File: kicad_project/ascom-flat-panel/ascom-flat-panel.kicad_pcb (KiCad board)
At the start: 4 copper layers, 55 x 29.5 mm, 13 parts, among them Q1 FQP30N06L, Q2 FQP30N06L

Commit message: optimisation (rotation de diode)
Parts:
- moved D2 10.2 mm to (109.0, 82.1), turned to 90 degrees
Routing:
- net SERVO GND: track 25.6 -> 27.7 mm
- net SERVO VCC: track 18.4 -> 16.9 mm
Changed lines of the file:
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@@
 			)
 		)
+		(model "C:/Users/dell/Documents/GitHub/ascom-flat-panel/kicad_project/seeeduino-xiao-samd21-3d-model/Seeeduino XIAO SAMD21 v4.step"
+			(offset
+				(xyz 0 0 0)
+			)
+			(scale
+				(xyz 1 1 1)
+			)
+			(rotate
+				(xyz -0 -0 -90)
+			)
+		)
 	)
 	(footprint "Diode_THT:D_DO-41_SOD81_P10.16mm_Horizontal"
@@
 	(footprint "Diode_THT:D_DO-41_SOD81_P10.16mm_Horizontal"
 		(layer "F.Cu")
-		(at 109 71.92 -90)
+		(at 109 82.08 90)
 		(descr "Diode, DO-41_SOD81 series, Axial, Horizontal, pin pitch=10.16mm, , length*diameter=5.2*2.7mm^2, , http://www.diodes.com/_files/packages/DO-41%20(Plastic).pdf")
 		(tags "Diode DO-41_SOD81 series Axial Horizontal pin pitch 10.16mm  length 5.2mm diameter 2.7mm")
 		(property "Reference" "D2"
-			(at 5.08 2.5 90)
+			(at 5.08 -2.5 90)
 			(layer "F.SilkS")
 			(effects
@@
 		)
 		(property "Datasheet" "http://www.vishay.com/docs/88503/1n4001.pdf"
-			(at 0 0 270)
+			(at 0 0 90)
 			(unlocked yes)
 			(layer "F.Fab")
@@
 		)
 		(property "Description" ""
-			(at 0 0 270)
+			(at 0 0 90)
 			(unlocked yes)
 			(layer "F.Fab")
@@
 		)
 		(property "Sim.Device" "D"
-			(at 0 0 270)
+			(at 0 0 90)
 			(unlocked yes)
 			(layer "F.Fab")
@@
 		)
 		(property "Sim.Pins" "1=K 2=A"
-			(at 0 0 270)
+			(at 0 0 90)
 			(unlocked yes)
 			(layer "F.Fab")
@@
 		(attr through_hole)
 		(fp_line
-			(start 2.36 1.47)
-			(end 7.8 1.47)
+			(start 7.8 -1.47)
+			(end 2.36 -1.47)
 			(stroke
 				(width 0.12)
@@
 		)
 		(fp_line
-			(start 7.8 1.47)
-			(end 7.8 -1.47)
+			(start 3.38 -1.47)
+			(end 3.38 1.47)
 			(stroke
 				(width 0.12)
@@
 		)
 		(fp_line
-			(start 1.34 0)
-			(end 2.36 0)
+			(start 3.26 -1.47)
+			(end 3.26 1.47)
 			(stroke
 				(width 0.12)
@@
 		)
 		(fp_line
-			(start 8.82 0)
-			(end 7.8 0)
+			(start 3.14 -1.47)
+			(end 3.14 1.47)
 			(stroke
 				(width 0.12)
@@
 		)
 		(fp_line
-			(start 3.14 -1.47)
-			(end 3.14 1.47)
+			(start 8.82 0)
+			(end 7.8 0)
 			(stroke
 				(width 0.12)
@@
 		)
 		(fp_line
-			(start 3.26 -1.47)
-			(end 3.26 1.47)
+			(start 1.34 0)
+			(end 2.36 0)
 			(stroke
 				(width 0.12)
@@
 		)
 		(fp_line
-			(start 3.38 -1.47)
-			(end 3.38 1.47)
+			(start 7.8 1.47)
+			(end 7.8 -1.47)
 			(stroke
 				(width 0.12)
@@
 		)
 		(fp_line
-			(start 7.8 -1.47)
-			(end 2.36 -1.47)
+			(start 2.36 1.47)
+			(end 7.8 1.47)
 			(stroke
 				(width 0.12)
@@
 		)
 		(fp_line
-			(start -1.35 1.6)
-			(end 11.51 1.6)
+			(start 11.51 -1.6)
+			(end -1.35 -1.6)
 			(stroke
 				(width 0.05)
@@
 		)
 		(fp_line
-			(start 11.51 1.6)
-			(end 11.51 -1.6)
+			(start -1.35 -1.6)
+			(end -1.35 1.6)
 			(stroke
 				(width 0.05)
@@
 		)
 		(fp_line
-			(start -1.35 -1.6)
-			(end -1.35 1.6)
+			(start 11.51 1.6)
+			(end 11.51 -1.6)
 			(stroke
 				(width 0.05)
@@
 		)
 		(fp_line
-			(start 11.51 -1.6)
-			(end -1.35 -1.6)
+			(start -1.35 1.6)
+			(end 11.51 1.6)
 			(stroke
 				(width 0.05)
@@
 		)
 		(fp_line
-			(start 2.48 1.35)
-			(end 7.68 1.35)
+			(start 7.68 -1.35)
+			(end 2.48 -1.35)
 			(stroke
 				(width 0.1)
@@
 		)
 		(fp_line
-			(start 7.68 1.35)
-			(end 7.68 -1.35)
+			(start 3.36 -1.35)
+			(end 3.36 1.35)
 			(stroke
 				(width 0.1)
@@
 		)
 		(fp_line
-			(start 0 0)
-			(end 2.48 0)
+			(start 3.26 -1.35)
+			(end 3.26 1.35)
 			(stroke
 				(width 0.1)
@@
 		)
 		(fp_line
-			(start 10.16 0)
-			(end 7.68 0)
+			(start 3.16 -1.35)
+			(end 3.16 1.35)
 			(stroke
 				(width 0.1)
@@
 		)
 		(fp_line
-			(start 3.16 -1.35)
-			(end 3.16 1.35)
+			(start 10.16 0)
+			(end 7.68 0)
 			(stroke
 				(width 0.1)
@@
 		)
 		(fp_line
-			(start 3.26 -1.35)
-			(end 3.26 1.35)
+			(start 0 0)
+			(end 2.48 0)
 			(stroke
 				(width 0.1)
@@
 		)
 		(fp_line
-			(start 3.36 -1.35)
-			(end 3.36 1.35)
+			(start 7.68 1.35)
+			(end 7.68 -1.35)
 			(stroke
 				(width 0.1)
@@
 		)
 		(fp_line
-			(start 7.68 -1.35)
-			(end 2.48 -1.35)
+			(start 2.48 1.35)
+			(end 7.68 1.35)
 			(stroke
 				(width 0.1)
@@
 		)
 		(pad "1" thru_hole rect
-			(at 0 0 270)
+			(at 0 0 90)
 			(size 2.2 2.2)
 			(drill 1.1)
@@
 		)
 		(pad "2" thru_hole oval
-			(at 10.16 0 270)
+			(at 10.16 0 90)
 			(size 2.2 2.2)
 			(drill 1.1)
@@
 	)
 	(segment
-		(start 109 76.58)
-		(end 114.5 82.08)
+		(start 114.5 82.08)
+		(end 109 82.08)
 		(width 0.4)
 		(layer "B.Cu")
@@
 	)
 	(segment
-		(start 109 71.92)
-		(end 104.5 71.92)
+		(start 103.5 73)
+		(end 103.5 72.92)
 		(width 0.4)
 		(layer "B.Cu")
@@
 	)
 	(segment
-		(start 109 71.92)
-		(end 109 76.58)
+		(start 109 78.5)
+		(end 103.5 73)
 		(width 0.4)
 		(layer "B.Cu")
@@
 	)
 	(segment
-		(start 104.5 71.92)
-		(end 103.5 72.92)
+		(start 109 82.08)
+		(end 109 78.5)
 		(width 0.4)
 		(layer "B.Cu")
@@
 	)
 	(segment
+		(start 102.299 74.259)
+		(end 103.5 75.46)
+		(width 0.4)
+		(layer "B.Cu")
+		(net 4)
+	)
+	(segment
+		(start 102.299 71.719)
+		(end 102.299 74.259)
+		(width 0.4)
+		(layer "B.Cu")
+		(net 4)
+	)
+	(segment
 		(start 102.299 76.661)
 		(end 103.5 75.46)
@@
 	)
 	(segment
-		(start 103.945 91)
-		(end 102.299 89.354)
+		(start 108.799 71.719)
+		(end 102.299 71.719)
 		(width 0.4)
 		(layer "B.Cu")
@@
 	)
 	(segment
-		(start 109 82.08)
-		(end 109 80.96)
+		(start 109 71.92)
+		(end 108.799 71.719)
 		(width 0.4)
 		(layer "B.Cu")
@@
 	)
 	(segment
-		(start 109 80.96)
-		(end 103.5 75.46)
+		(start 103.945 91)
+		(end 102.299 89.354)
 		(width 0.4)
 		(layer "B.Cu")

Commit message: correction suite à détection d'erreur...
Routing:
- net SERVO POSITION CONTROL: track 21.3 -> 22.4 mm
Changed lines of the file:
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@@
 	)
 	(segment
-		(start 111.980397 86.971)
-		(end 103.5 78.490603)
+		(start 111.537339 86.971)
+		(end 108.566339 84)
+		(width 0.2)
+		(layer "B.Cu")
+		(net 6)
+	)
+	(segment
+		(start 108.566339 84)
+		(end 108 84)
 		(width 0.2)
 		(layer "B.Cu")
@@
 	(segment
 		(start 119.009 86.971)
-		(end 111.980397 86.971)
+		(end 111.537339 86.971)
 		(width 0.2)
 		(layer "B.Cu")
@@
 		(width 0.2)
 		(layer "B.Cu")
+		(net 6)
+	)
+	(segment
+		(start 105.5 81.5)
+		(end 105.5 80)
+		(width 0.2)
+		(layer "B.Cu")
+		(net 6)
+	)
+	(segment
+		(start 105.5 80)
+		(end 103.5 78)
+		(width 0.2)
+		(layer "B.Cu")
+		(net 6)
+	)
+	(segment
+		(start 108 84)
+		(end 105.5 81.5)
+		(width 0.2)
+		(layer "B.Cu")

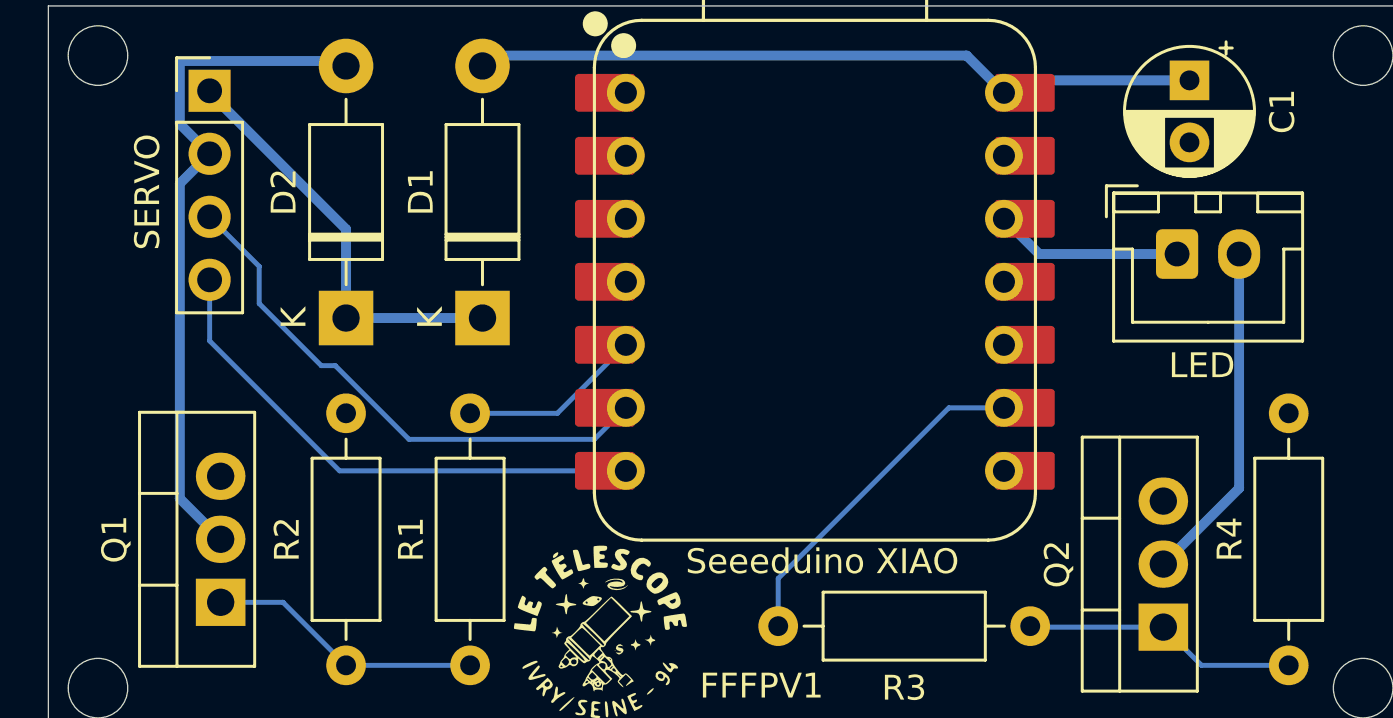
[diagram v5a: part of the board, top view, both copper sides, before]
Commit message: Corrections de routage pour améliorer les connexions à la masse
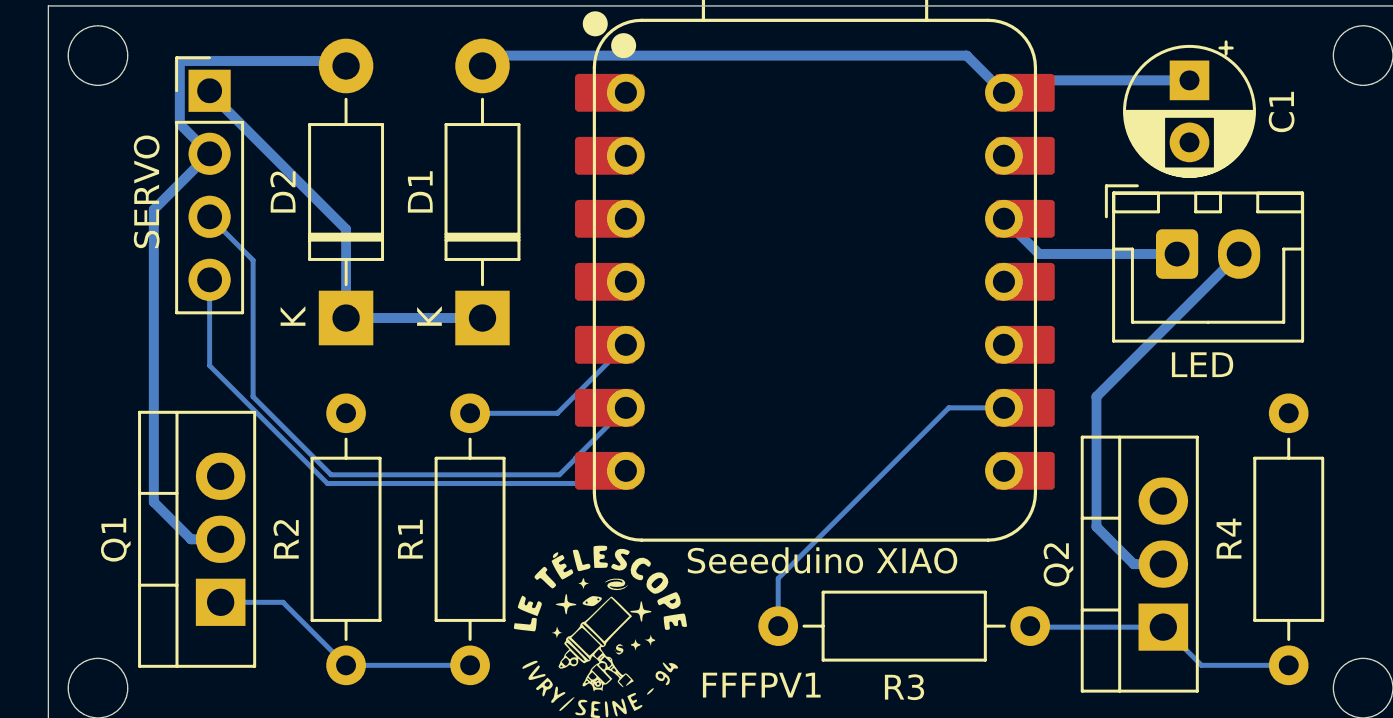
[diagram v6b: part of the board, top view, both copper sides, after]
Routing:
- net SERVO POSITION CONTROL: track 22.4 -> 25.9 mm
- net Net-(J3-Pin_2): track 13.8 -> 16.7 mm
- net SERVO GND: track 27.7 -> 29.3 mm
- net SERVO POSITION FEEDBACK: track 21.4 -> 22.4 mm
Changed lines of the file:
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@@
 	)
 	(segment
-		(start 102.299 76.661)
-		(end 103.5 75.46)
+		(start 108.799 71.719)
+		(end 102.299 71.719)
 		(width 0.4)
 		(layer "B.Cu")
@@
 	)
 	(segment
-		(start 108.799 71.719)
-		(end 102.299 71.719)
+		(start 101.25 89.5)
+		(end 101.25 77.71)
 		(width 0.4)
 		(layer "B.Cu")
@@
 	)
 	(segment
-		(start 103.945 91)
-		(end 102.299 89.354)
+		(start 101.25 77.71)
+		(end 103.5 75.46)
 		(width 0.4)
 		(layer "B.Cu")
@@
 	)
 	(segment
-		(start 102.299 89.354)
-		(end 102.299 76.661)
+		(start 103.945 91)
+		(end 102.75 91)
 		(width 0.4)
 		(layer "B.Cu")
@@
 	)
 	(segment
-		(start 120.28 88.24)
-		(end 108.74 88.24)
+		(start 102.75 91)
+		(end 101.25 89.5)
+		(width 0.4)
+		(layer "B.Cu")
+		(net 4)
+	)
+	(segment
+		(start 119.77 88.75)
+		(end 108.25 88.75)
 		(width 0.2)
 		(layer "B.Cu")
@@
 	)
 	(segment
-		(start 103.5 83)
-		(end 103.5 80.54)
+		(start 108.25 88.75)
+		(end 103.5 84)
 		(width 0.2)
 		(layer "B.Cu")
@@
 	)
 	(segment
-		(start 108.74 88.24)
-		(end 103.5 83)
+		(start 120.28 88.24)
+		(end 119.77 88.75)
+		(width 0.2)
+		(layer "B.Cu")
+		(net 5)
+	)
+	(segment
+		(start 103.5 84)
+		(end 103.5 80.54)
 		(width 0.2)
 		(layer "B.Cu")
@@
 	)
 	(segment
-		(start 111.537339 86.971)
-		(end 108.566339 84)
+		(start 117.601 88.399)
+		(end 118.25 87.75)
 		(width 0.2)
 		(layer "B.Cu")
@@
 	)
 	(segment
-		(start 108.566339 84)
-		(end 108 84)
+		(start 118.25 87.73)
+		(end 120.28 85.7)
 		(width 0.2)
 		(layer "B.Cu")
@@
 	)
 	(segment
-		(start 119.009 86.971)
-		(end 111.537339 86.971)
+		(start 103.5 78)
+		(end 105.25 79.75)
 		(width 0.2)
 		(layer "B.Cu")
@@
 	)
 	(segment
-		(start 120.28 85.7)
-		(end 119.009 86.971)
+		(start 108.399 88.399)
+		(end 117.601 88.399)
 		(width 0.2)
 		(layer "B.Cu")
@@
 	)
 	(segment
-		(start 105.5 81.5)
-		(end 105.5 80)
+		(start 105.25 85.25)
+		(end 108.399 88.399)
 		(width 0.2)
 		(layer "B.Cu")
@@
 	)
 	(segment
-		(start 105.5 80)
-		(end 103.5 78)
+		(start 105.25 79.75)
+		(end 105.25 85.25)
 		(width 0.2)
 		(layer "B.Cu")
@@
 	)
 	(segment
-		(start 108 84)
-		(end 105.5 81.5)
-		(width 0.2)
+		(start 118.25 87.75)
+		(end 118.25 87.73)
+		(width 0.15)
 		(layer "B.Cu")
 		(net 6)
@@
 	)
 	(segment
-		(start 141.945 92)
-		(end 145 88.945)
+		(start 139.25 85.25)
+		(end 145 79.5)
 		(width 0.4)
 		(layer "B.Cu")
@@
 	)
 	(segment
-		(start 145 88.945)
-		(end 145 79.5)
+		(start 140.75 92)
+		(end 139.25 90.5)
 		(width 0.4)
 		(layer "B.Cu")
+		(net 8)
+	)
+	(segment
+		(start 141.945 92)
+		(end 140.75 92)
+		(width 0.4)
+		(layer "B.Cu")
+		(net 8)
+	)
+	(segment
+		(start 139.25 90.5)
+		(end 139.25 85.25)
+		(width 0.4)
+		(layer "B.Cu")

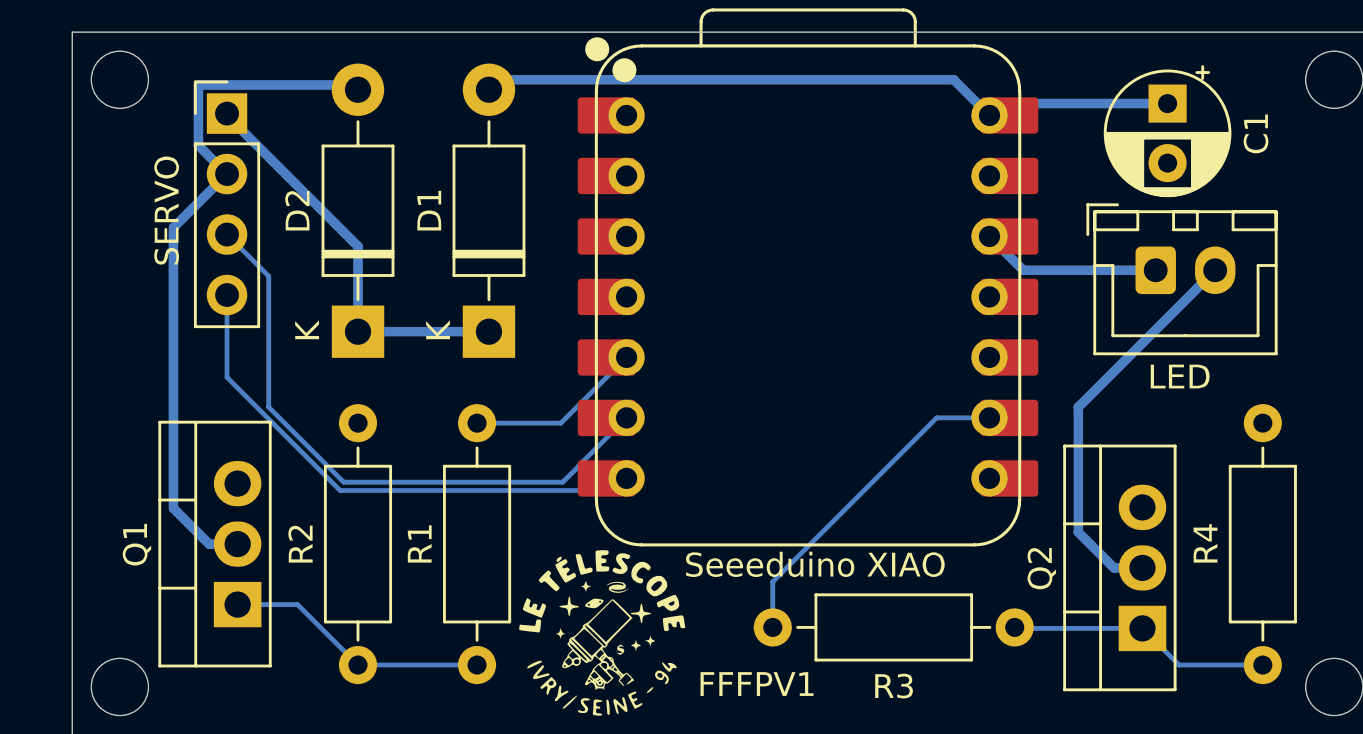
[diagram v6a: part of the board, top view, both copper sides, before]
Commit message: Mise à jour des références des diodes et MOSFET suivant composants achetés. TODO : vérifier pas et diamètre de C1 - ajuster empreinte le cas échéant
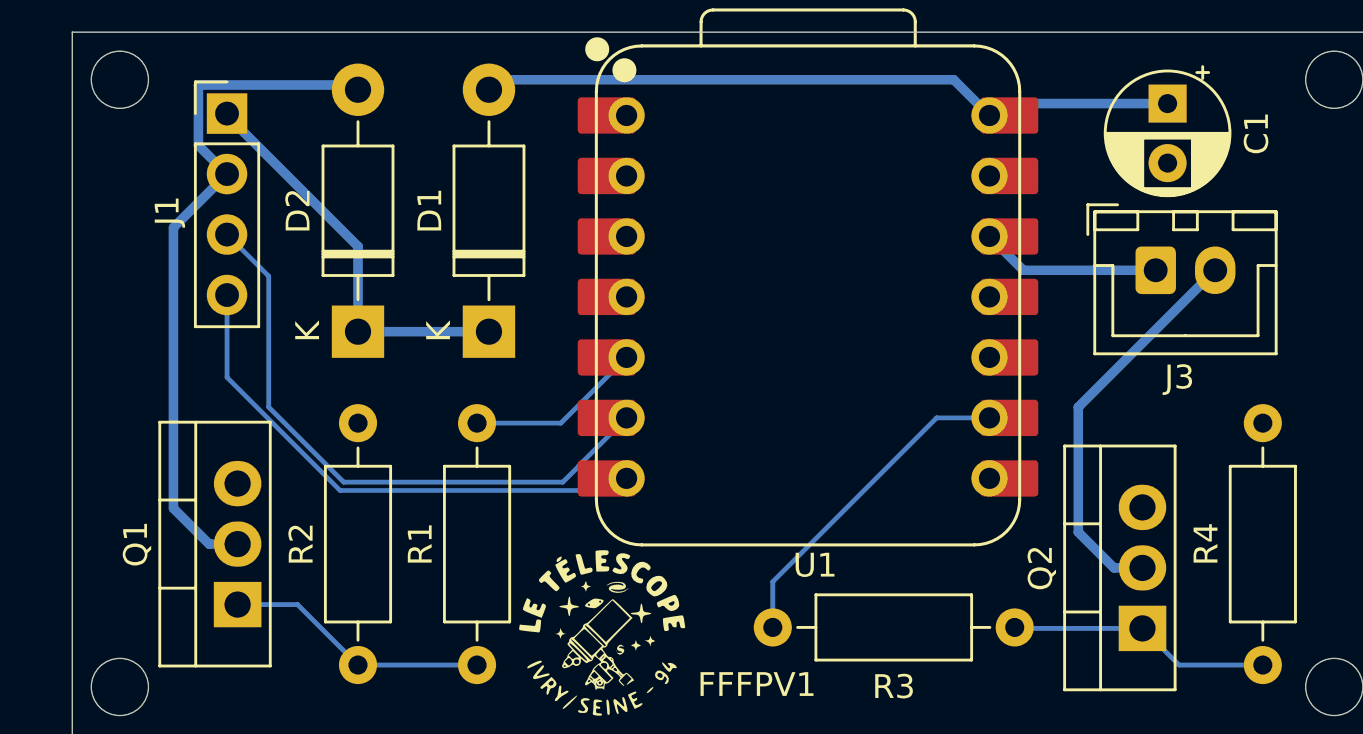
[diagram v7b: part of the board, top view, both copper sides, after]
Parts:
- D1: value 1N5817 -> 1N5819
- D2: value 1N4001 -> 1N4007
- Q1, Q2: value FQP30N06L -> IRLZ34N
- U1: renamed from Seeeduino XIAO
- renumbered SERVO to J1, LED to J3
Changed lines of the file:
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@@
 		(layer "F.Cu")
 		(at 128 80.5575)
-		(property "Reference" "Seeeduino XIAO"
+		(property "Reference" "U1"
 			(at 0.2 11.3425 0)
 			(unlocked yes)
@@
 			)
 		)
-		(property "Value" "1N5817"
+		(property "Value" "1N5819"
 			(at 5.08 2.47 90)
 			(layer "F.Fab")
@@
 			)
 		)
-		(property "Value" "FQP30N06L"
+		(property "Value" "IRLZ34N"
 			(at 2.54 2.5 90)
 			(layer "F.Fab")
@@
 			)
 		)
-		(property "Value" "1N4001"
+		(property "Value" "1N4007"
 			(at 5.08 2.47 90)
 			(layer "F.Fab")
@@
 			)
 		)
-		(property "Value" "FQP30N06L"
+		(property "Value" "IRLZ34N"
 			(at 2.54 2.5 90)
 			(layer "F.Fab")
@@
 		(descr "JST XH series connector, B2B-XH-A (http://www.jst-mfg.com/product/pdf/eng/eXH.pdf), generated with kicad-footprint-generator")
 		(tags "connector JST XH vertical")
-		(property "Reference" "LED"
+		(property "Reference" "J3"
 			(at 1 4.5 180)
 			(layer "F.SilkS")
@@
 		(descr "Through hole straight pin header, 1x04, 2.54mm pitch, single row")
 		(tags "Through hole pin header THT 1x04 2.54mm single row")
-		(property "Reference" "SERVO"
+		(property "Reference" "J1"
 			(at -2.5 4.08 90)
 			(layer "F.SilkS")

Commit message: ajout logo club en gros sur couche inférieure
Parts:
- added G***: LOGO, LOGO, B.Cu at (127.9, 78.8)
